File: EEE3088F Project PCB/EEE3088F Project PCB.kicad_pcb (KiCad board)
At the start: 2 copper layers, 76 x 53 mm, 52 parts, among them IC1 74LVC1G04SE-7, J1 JST PH 2.00mm connector, J2 TYPE-C-31-M-12, SW1 SS12D07VG5 087, U1 DRV8833PWR, U10 LM7805_TO220, U11 TC4056A., U2 DRV8833PWPR, U3 INA219AxD, U4 CH224K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

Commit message: Added student numbers, corrected board boundries, placed connectors (USB, JST, & pin headers)
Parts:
- J1: value JST PH 2.00mm connector -> JST PH
- J2: value TYPE-C-31-M-12 -> USB C
- moved C2 118.4 mm to (65.6, 37.8)
- moved R_PROG_1 118.4 mm to (69.8, 24.3)
- moved 0.16 118.4 mm to (85.4, 20.3)
- moved C1 118.4 mm to (60.4, 37.8)
- moved C10 118.4 mm to (30.9, 32.3)
- moved C11 118.4 mm to (20.4, 24.3)
- moved C12 118.4 mm to (37.9, 33.3)
- moved C13 118.4 mm to (26.4, 18.8)
- moved C14 118.4 mm to (54.4, 38.2)
- moved C15 118.4 mm to (26.9, 23.8)
- moved C16 118.4 mm to (38.3, 18.3)
- moved C17 118.4 mm to (20.4, 18.8)
- moved C18 118.4 mm to (44.9, 18.3)
- moved C19 118.4 mm to (38.4, 48.8)
- moved C20 118.4 mm to (54.4, 44.3)
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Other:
- board size 76 x 53 mm -> 80 x 54.9 mm
- board text added: "TRKJON002 & MTMTAD006"

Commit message: added fault managment and testing points for USB Integration and Charging requirments
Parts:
- added JP1: SolderJumper_2_Bridged, Jumper:SolderJumper-2_P1.3mm_Bridged2Bar_Pad1.0x1.5mm, F.Cu at (163.2, 87.5)
- added R21: 0.16, exported_footprints:CAPC3216X180N, F.Cu at (38.5, 58.5)
- added R6: 200m, Resistor_SMD:R_Shunt_Vishay_WSR2_WSR3, F.Cu at (151.5, 64.5)
- added TP1: TestPoint, TestPoint:TestPoint_Pad_1.0x1.0mm, F.Cu at (176.0, 100.5)
- added TP2: TestPoint, TestPoint:TestPoint_Pad_1.0x1.0mm, F.Cu at (177.0, 66.5)
- added TP3: TestPoint, TestPoint:TestPoint_Pad_2.0x2.0mm, F.Cu at (187.5, 108.5)
- added TP4: TestPoint, TestPoint:TestPoint_Pad_1.0x1.0mm, F.Cu at (196.0, 104.5)
- added TP7: TestPoint, TestPoint:TestPoint_Pad_1.0x1.0mm, F.Cu at (177.0, 69.5)
- C19: value 0.22u -> 0.33u
- J1: value JST PH -> JST PH 2.00mm connector
- J2: value USB C -> TYPE-C-31-M-12; footprint exported_footprints:HRO_TYPE-C-31-M-12 -> exported_footprints:TYPE-C-31-M-12
- U10: value LM7805_TO220 -> LM7805L-TF3-T
- moved R4 159.3 mm to (175.5, 105.0), turned to 90 degrees
- moved R3 158.8 mm to (170.0, 108.0), turned to 180 degrees
- moved C8 151.9 mm to (162.0, 101.5), turned to -90 degrees
- moved U4 149.3 mm to (170.0, 102.5)
- moved C21 136.5 mm to (162.0, 91.9), turned to 90 degrees
- moved C19 132.3 mm to (162.0, 96.0), turned to -90 degrees
- moved U10 126.6 mm to (156.0, 98.0), turned to 90 degrees
- moved C20 110.0 mm to (155.5, 87.5)
- moved U11 96.1 mm to (170.5, 94.0)
- moved J2 6.84 mm to (159.6, 110.1)
- moved am1 1.09 mm to (210.8, 115.0)
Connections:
- net /VBUS_R3 renamed /VDD
- C21 pad 2: /Battery -> Net-(U11-BAT)
- C7 pad 1: /I2C1_SCL -> /Battery
- J2 pad A5: Net-(J2-CC1) -> /CC1
- J2 pad A6: Net-(U4-DP) -> /DP
- J2 pad A7: Net-(U4-DM) -> /DN
- J2 pad B5: Net-(J2-CC2) -> /CC2
- J2 pad B6: Net-(U4-DP) -> /DP
- J2 pad B7: Net-(U4-DM) -> /DN
- R1 pad 2: /I2C1_SCL -> /Battery
- R2 pad 1: /I2C1_SCL -> /Battery
- U11 pad 4: /V_BATT_CHARGE -> Net-(JP1-B)
- U11 pad 5: /Battery -> Net-(U11-BAT)
- U3 pad 5: /I2C1_SCL -> /Battery
- am1 pad 16: /I2C1_SCL -> /Battery
- am1 pad 17: /I2C1_SCL -> /Battery

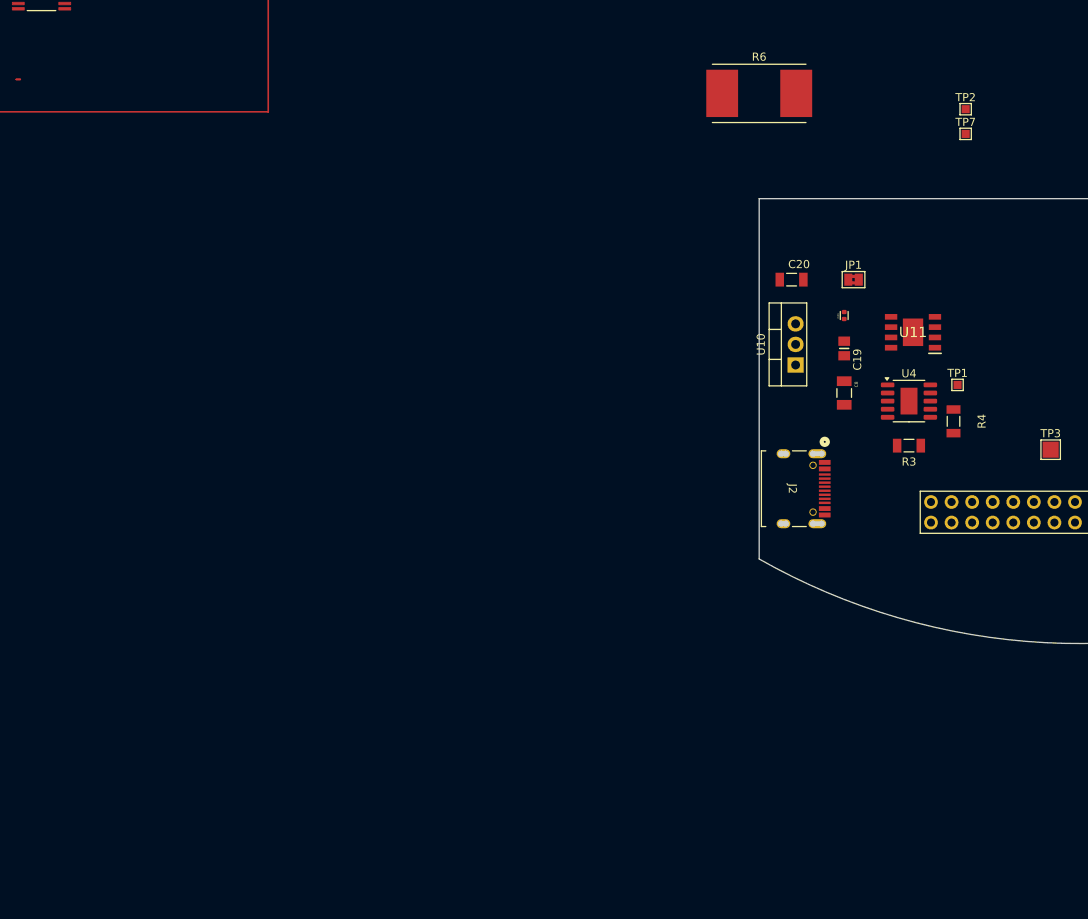
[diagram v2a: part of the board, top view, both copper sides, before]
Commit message: ajusted some testing points and added footprints for USB integration + half of the charging requirments
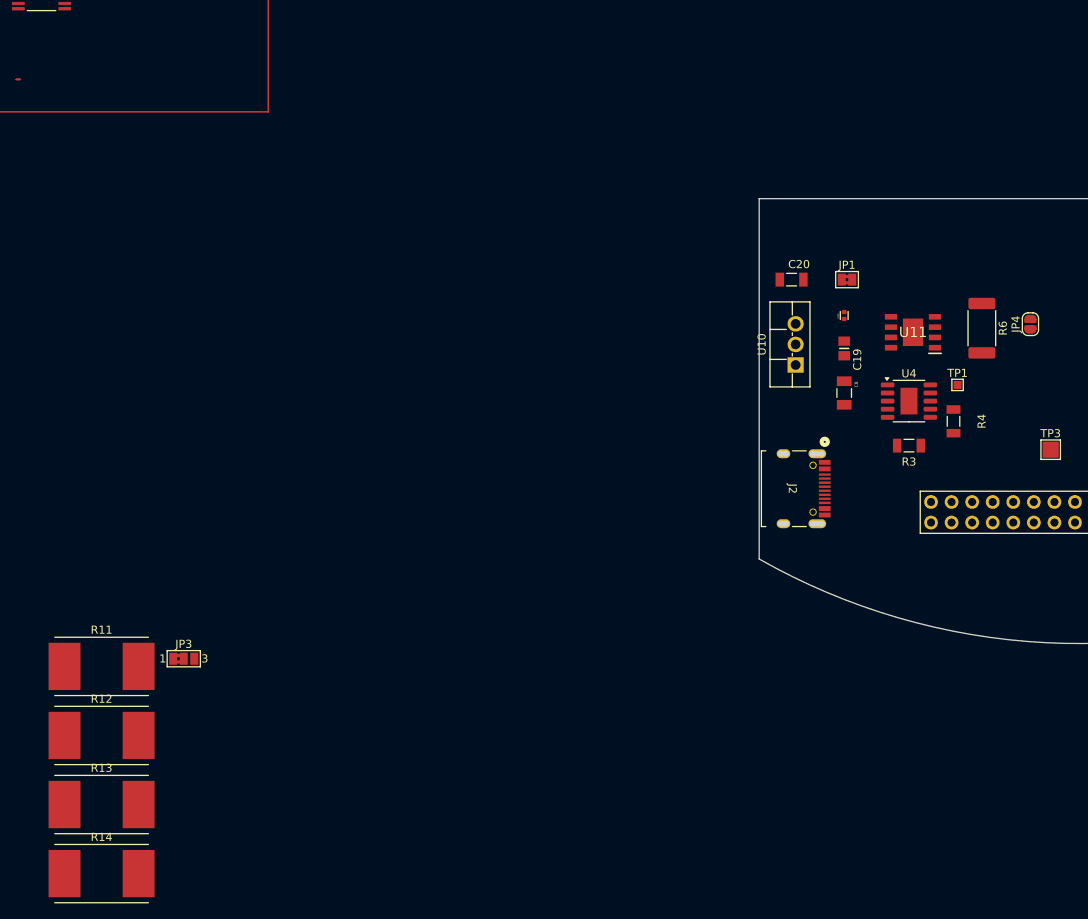
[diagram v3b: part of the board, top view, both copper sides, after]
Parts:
- removed TP2, TP7: TestPoint, TestPoint:TestPoint_Pad_1.0x1.0mm
- added JP3: R_PROG_2 Bridge, Jumper:SolderJumper-3_P1.3mm_Bridged2Bar12_Pad1.0x1.5mm_NumberLabels, F.Cu at (80.4, 134.3)
- added JP4: SolderJumper_2_Open, Jumper:SolderJumper-2_P1.3mm_Open_RoundedPad1.0x1.5mm, F.Cu at (185.0, 93.0)
- added R11: 200m, Resistor_SMD:R_Shunt_Vishay_WSR2_WSR3, F.Cu at (70.3, 135.3)
- added R12: 200m, Resistor_SMD:R_Shunt_Vishay_WSR2_WSR3, F.Cu at (70.3, 143.8)
- added R13: 200m, Resistor_SMD:R_Shunt_Vishay_WSR2_WSR3, F.Cu at (70.3, 152.3)
- added R14: 200m, Resistor_SMD:R_Shunt_Vishay_WSR2_WSR3, F.Cu at (70.3, 160.9)
- JP1: value SolderJumper_2_Bridged -> V_BATT_CHRG Bridge
- R6: value 200m -> 160m; footprint Resistor_SMD:R_Shunt_Vishay_WSR2_WSR3 -> Resistor_SMD:R_2512_6332Metric_Pad1.40x3.35mm_HandSolder
- TP1: value TestPoint -> HV Test Point
- U10: footprint Package_TO_SOT_THT:TO-220-3_Vertical -> Package_TO_SOT_THT:TO-220F-3_Vertical
- moved R6 40.0 mm to (179.0, 93.5), turned to -90 degrees
- moved JP1 0.80 mm to (162.3, 87.5)
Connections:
- net /V_BATT_CHARGE renamed /V_BATT_CHRG
- R_PROG_1 pad 1: Net-(S1-1Z) -> Net-(JP2-A)
- R_PROG_2 pad 2: Net-(S1-2Z) -> Net-(JP3-C)
- S1 pad 2: Net-(S1-1Z) -> Net-(JP2-C)
- S1 pad 6: Net-(S1-2Z) -> Net-(JP3-A)
- U1 pad 2: /MOTOR1_A_OUT -> Net-(U1-AOUT1)
- U1 pad 7: /Motor2_A_OUT -> Net-(U1-BOUT1)
- U2 pad 2: /MOTOR3_A_OUT -> Net-(U2-AOUT1)
- U2 pad 7: /Motor4_A_OUT -> Net-(U2-BOUT1)

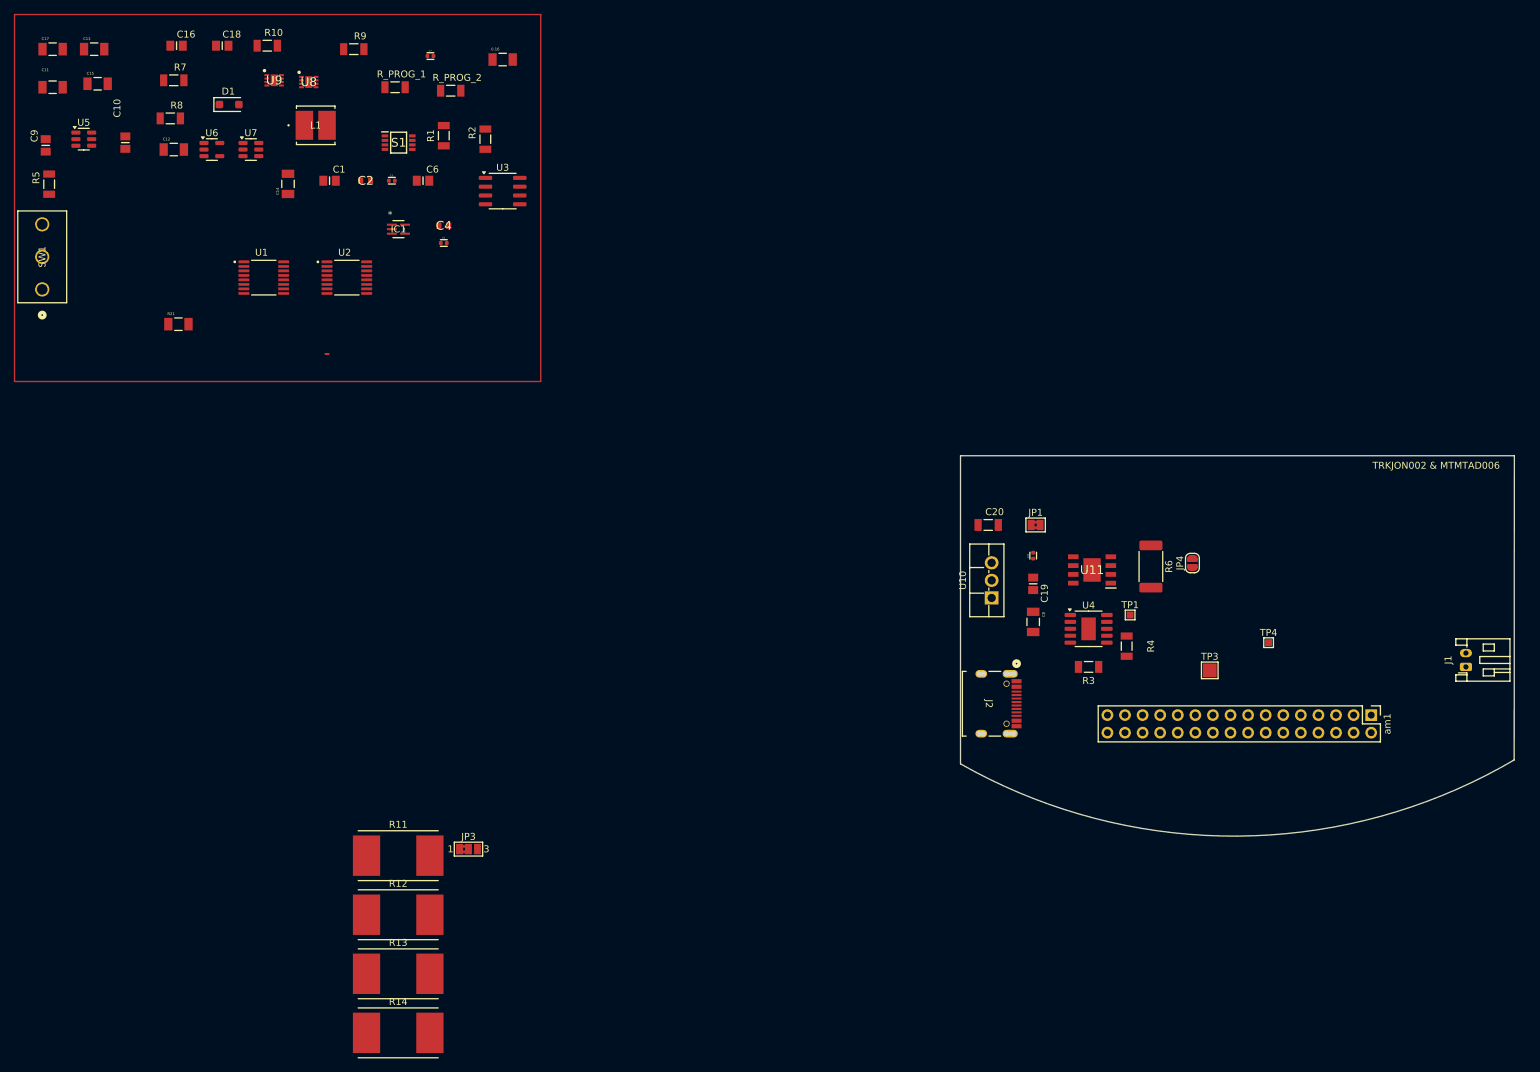
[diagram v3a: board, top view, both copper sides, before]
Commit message: added footprints to all my componets, placed all components on the board, and added all my jlcpcb part numbers
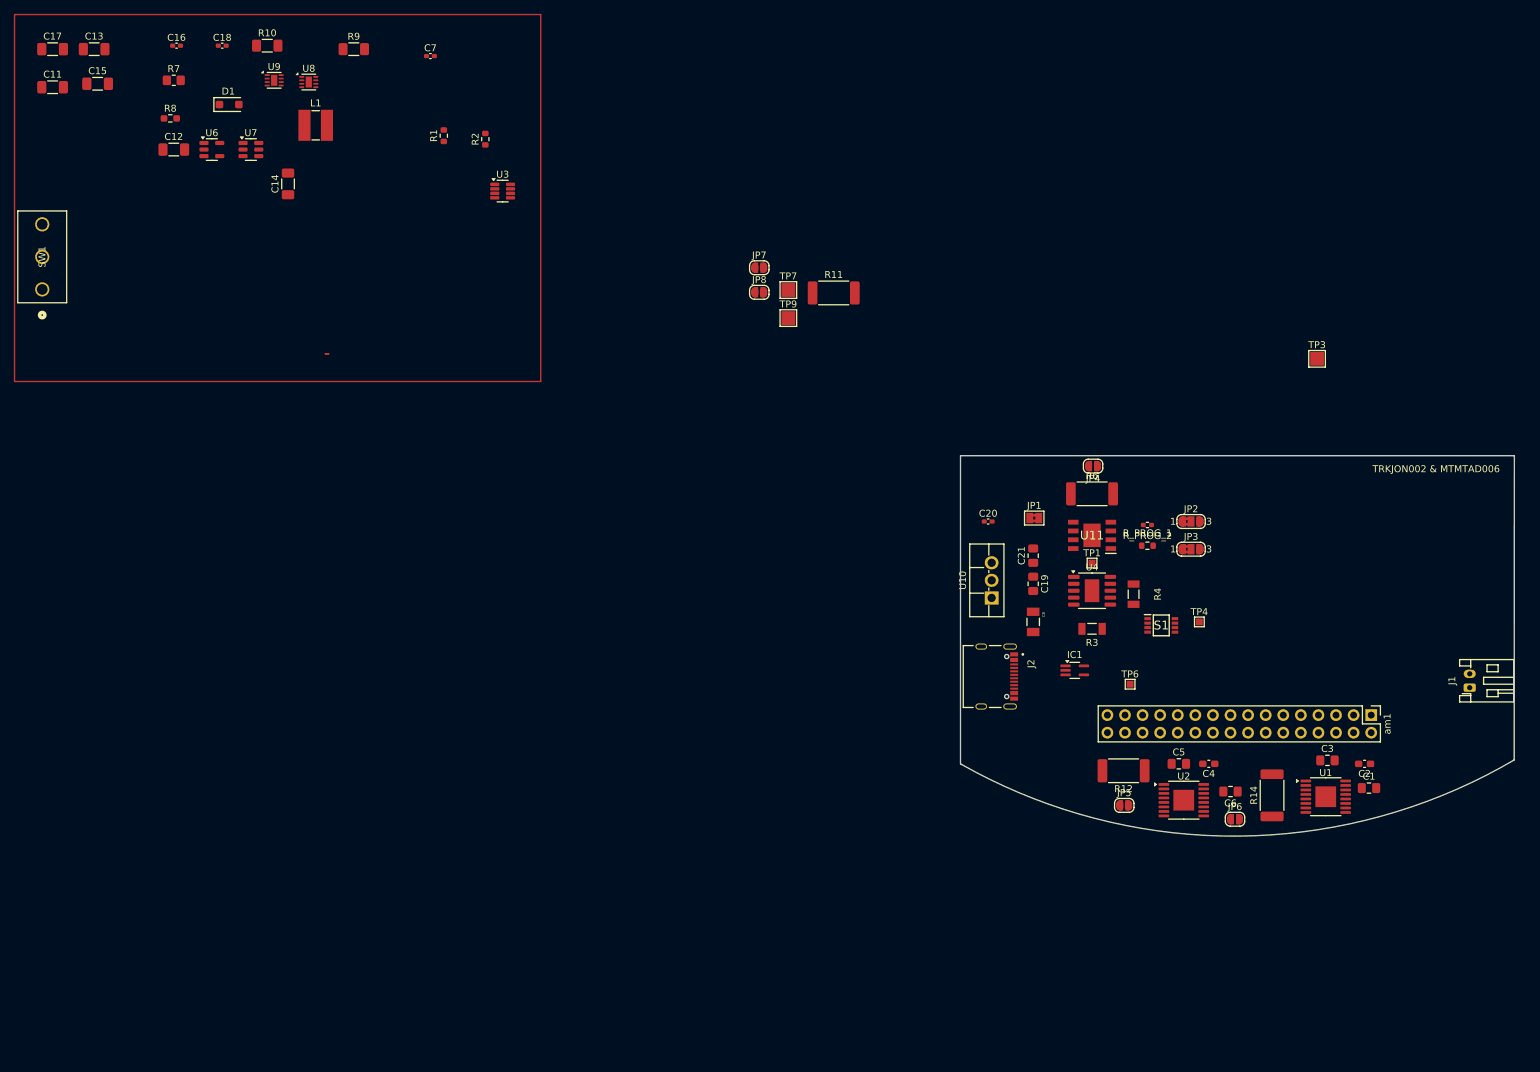
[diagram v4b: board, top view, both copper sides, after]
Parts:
- removed 0.16: R_Shunt, exported_footprints:CAPC3216X180N
- removed C10: 220uF, exported_footprints:CAPC2012X140N
- removed C9: 22uF, exported_footprints:CAPC2012X140N
- removed R13: 200m, Resistor_SMD:R_Shunt_Vishay_WSR2_WSR3
- removed R21: 0.16, exported_footprints:CAPC3216X180N
- removed R5: 10, exported_footprints:RESC3115X65N
- removed U5: TPS22918, Package_TO_SOT_SMD:SOT-23-6
- added JP2: R_PROG_1 Bridge, Jumper:SolderJumper-3_P1.3mm_Bridged2Bar12_RoundedPad1.0x1.5mm_NumberLabels, F.Cu at (184.8, 87.0)
- added JP5: SolderJumper_2_Open, Jumper:SolderJumper-2_P1.3mm_Open_RoundedPad1.0x1.5mm, F.Cu at (175.2, 128.0)
- added JP6: SolderJumper_2_Open, Jumper:SolderJumper-2_P1.3mm_Open_RoundedPad1.0x1.5mm, F.Cu at (191.2, 130.0)
- added JP7: SolderJumper_2_Open, Jumper:SolderJumper-2_P1.3mm_Open_RoundedPad1.0x1.5mm, F.Cu at (122.4, 50.3)
- added JP8: SolderJumper_2_Open, Jumper:SolderJumper-2_P1.3mm_Open_RoundedPad1.0x1.5mm, F.Cu at (122.4, 53.9)
- added TP6: TestPoint, TestPoint:TestPoint_Pad_1.0x1.0mm, F.Cu at (176.0, 110.5)
- added TP7: TestPoint, TestPoint:TestPoint_Pad_2.0x2.0mm, F.Cu at (126.6, 53.6)
- added TP9: TestPoint, TestPoint:TestPoint_Pad_2.0x2.0mm, F.Cu at (126.6, 57.6)
- C1, C19, C6: footprint exported_footprints:CAPC2012X140N -> Capacitor_SMD:C_0805_2012Metric_Pad1.18x1.45mm_HandSolder
- C11, C12, C13, C14, C15, C17: footprint exported_footprints:CAPC3216X180N -> Capacitor_SMD:C_1206_3216Metric_Pad1.33x1.80mm_HandSolder
- C16, C18: footprint exported_footprints:CAPC2012X140N -> Capacitor_SMD:C_0402_1005Metric_Pad0.74x0.62mm_HandSolder
- C2, C4: footprint exported_footprints:CAPC1608X90N -> Capacitor_SMD:C_0603_1608Metric_Pad1.08x0.95mm_HandSolder
- C20: footprint exported_footprints:RESC3115X65N -> Capacitor_SMD:C_0402_1005Metric_Pad0.74x0.62mm_HandSolder
- C21, C3, C5: footprint exported_footprints:CAPC1005X55N -> Capacitor_SMD:C_0805_2012Metric_Pad1.18x1.45mm_HandSolder
- C7: footprint exported_footprints:CAPC1005X55N -> Capacitor_SMD:C_0402_1005Metric_Pad0.74x0.62mm_HandSolder
- IC1: footprint exported_footprints:74LVC1G04SE-7 -> Package_TO_SOT_SMD:SOT-353_SC-70-5_Handsoldering
- J2: value TYPE-C-31-M-12 -> ~; footprint exported_footprints:TYPE-C-31-M-12 -> exported_footprints:HRO_TYPE-C-31-M-12
- JP3: footprint Jumper:SolderJumper-3_P1.3mm_Bridged2Bar12_Pad1.0x1.5mm_NumberLabels -> Jumper:SolderJumper-3_P1.3mm_Bridged2Bar12_RoundedPad1.0x1.5mm_NumberLabels
- L1: footprint exported_footprints:SMNR5040-220MT -> Inductor_SMD:L_Ferrocore_DLG-0403
- R1, R2: footprint exported_footprints:RESC3115X65N -> Resistor_SMD:R_0603_1608Metric
- R10, R9: footprint exported_footprints:RESC3115X65N -> Resistor_SMD:R_1206_3216Metric_Pad1.30x1.75mm_HandSolder
- R11, R12, R14: value 200m -> 160m; footprint Resistor_SMD:R_Shunt_Vishay_WSR2_WSR3 -> Resistor_SMD:R_2512_6332Metric_Pad1.40x3.35mm_HandSolder
- R7: footprint exported_footprints:RESC3115X65N -> Resistor_SMD:R_0805_2012Metric_Pad1.20x1.40mm_HandSolder
- R8: footprint exported_footprints:RESC3115X65N -> Resistor_SMD:R_0603_1608Metric_Pad0.98x0.95mm_HandSolder
- R_PROG_1: footprint exported_footprints:RESC3115X65N -> Resistor_SMD:R_0402_1005Metric_Pad0.72x0.64mm_HandSolder
- R_PROG_2: value 8K -> 6.2k; footprint exported_footprints:RESC3115X65N -> Resistor_SMD:R_0603_1608Metric
- U1, U2: footprint exported_footprints:SOP65P640X120-16N -> Package_SO:TSSOP-16-1EP_4.4x5mm_P0.65mm_EP3x3mm
- U3: footprint Package_SO:SOIC-8_3.9x4.9mm_P1.27mm -> Package_TO_SOT_SMD:TSOT-23-8
- U8, U9: footprint exported_footprints:SON50P200X200X80-9N -> Package_DFN_QFN:DFN-8-1EP_2x2mm_P0.5mm_EP0.9x1.6mm
- moved C1 173.9 mm to (210.5, 125.5)
- moved U1 170.7 mm to (204.2, 126.8)
- moved C2 167.1 mm to (209.9, 122.0), turned to 180 degrees
- moved C3 159.0 mm to (204.5, 121.5)
- moved C6 146.2 mm to (190.5, 126.0), turned to 180 degrees
- moved U2 142.5 mm to (183.8, 127.2)
- moved C4 135.1 mm to (187.4, 122.0), turned to 180 degrees
- moved R14 130.8 mm to (196.5, 126.5), turned to 90 degrees
- moved S1 130.4 mm to (180.5, 102.0)
- moved C5 130.1 mm to (183.0, 122.0)
- moved R_PROG_1 125.7 mm to (178.5, 87.5), turned to 180 degrees
- moved R_PROG_2 120.2 mm to (178.5, 90.5)
- moved IC1 116.6 mm to (168.0, 108.5)
- moved JP3 113.0 mm to (184.8, 91.0)
- moved R12 106.8 mm to (175.1, 123.0), turned to 180 degrees
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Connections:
- C1 pad 1: /Battery -> /V_sensing
- C3 pad 2: /Battery -> /V_sensing
- C6 pad 1: /Battery -> /V_sensing
- C7 pad 1: /Battery -> /V_switch
- R1 pad 2: /Battery -> /I2C1_SDA
- R11 pad 1: Net-(U1-AOUT1) -> /V_sensing
- R11 pad 2: /MOTOR1_A_OUT -> /V_switch
- R2 pad 1: /Battery -> /I2C1_SCL
- SW1 pad 1: /V_sensing -> GND
- SW1 pad 2: GND -> /V_switch
- SW1 pad 3: /ON -> /Battery
- U1 pad 12: /Battery -> /V_sensing
- U1 pad 2: Net-(U1-AOUT1) -> /MOTOR1_A_OUT
- U1 pad 7: Net-(U1-BOUT1) -> /Motor2_A_OUT
- U3 pad 5: /Battery -> /V_switch
- U3 pad 7: Net-(U3-IN-) -> /V_sensing
- U3 pad 8: Net-(U3-IN+) -> /V_switch
- am1 pad 16: /Battery -> /I2C1_SCL
- am1 pad 17: /Battery -> /I2C1_SDA
